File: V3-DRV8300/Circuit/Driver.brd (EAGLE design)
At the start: 63.5 x 55.5 mm, 37 parts, among them IC1 DRV8303DCA

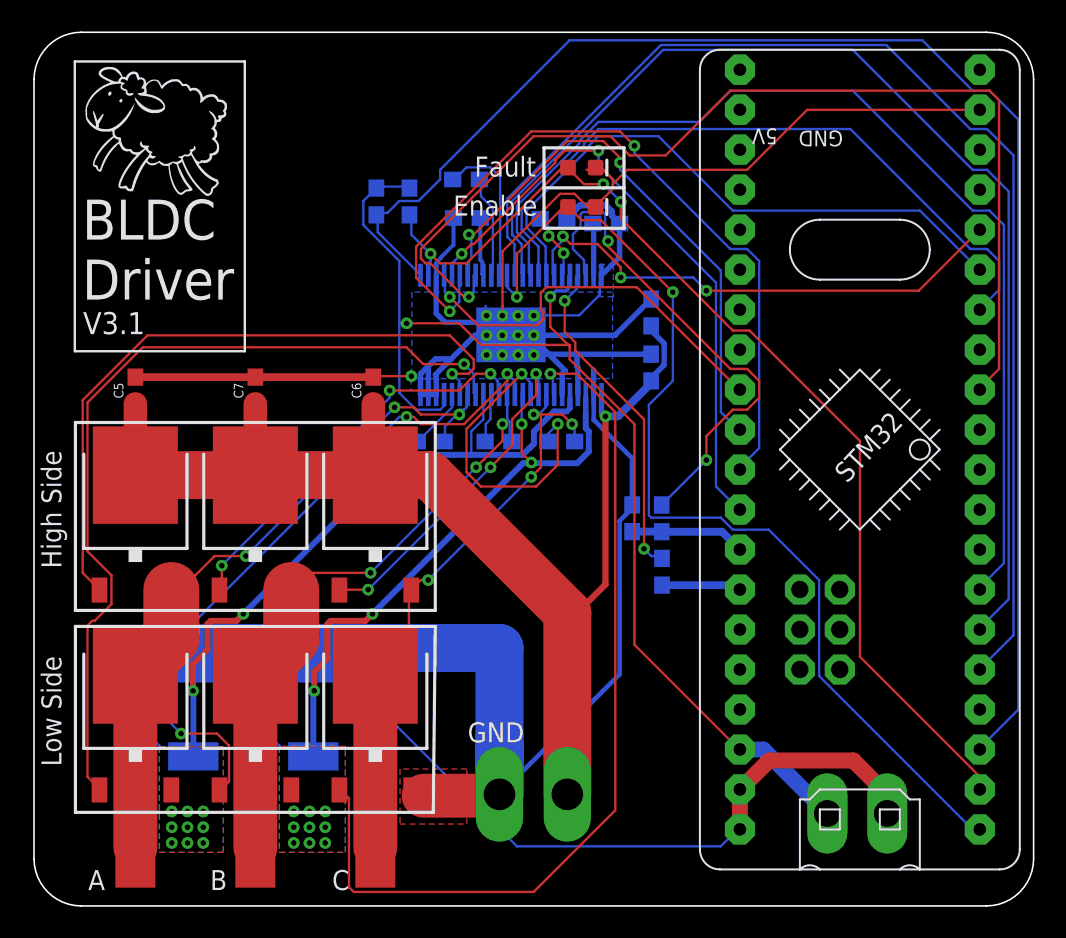
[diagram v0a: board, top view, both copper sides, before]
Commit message: Changed all the PWM output pin to the same timer, Added 2 selector for C.S.A.
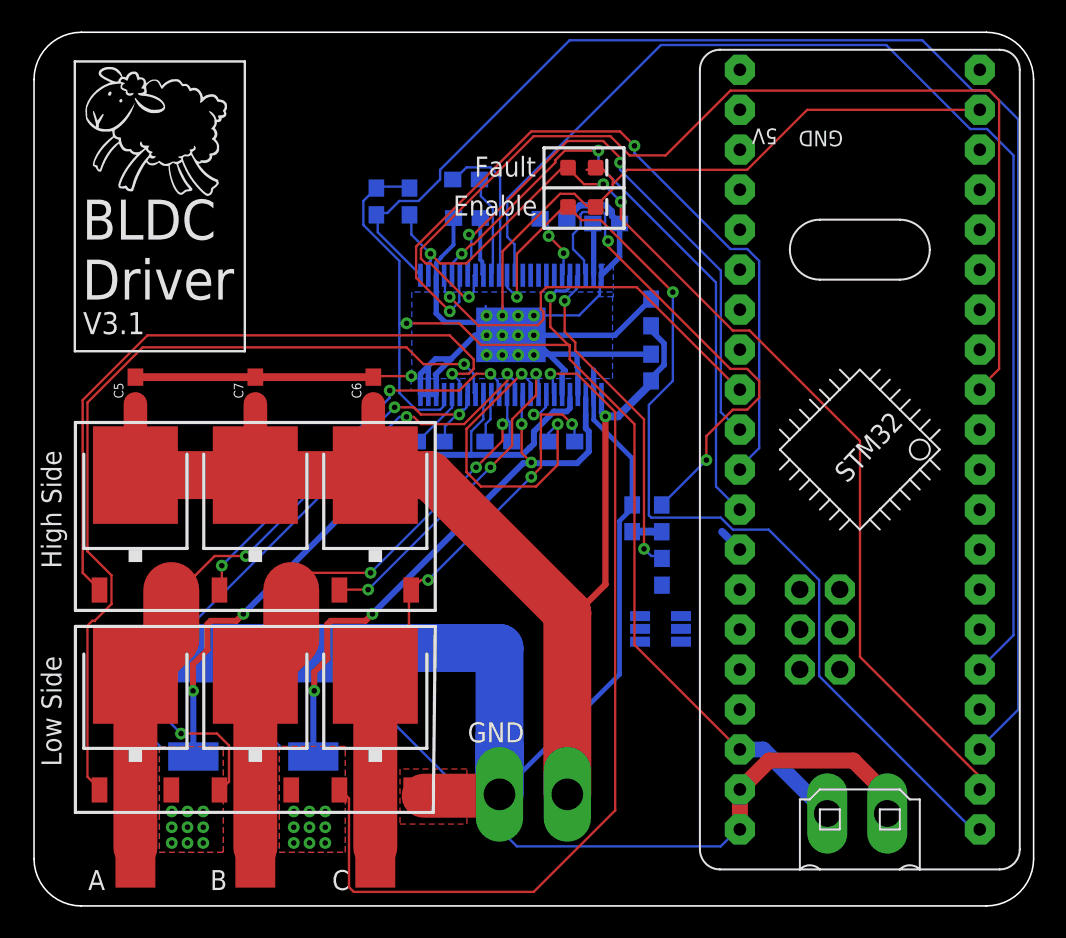
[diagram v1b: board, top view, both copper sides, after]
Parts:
- added SO1_SELECTOR, SO2_SELECTOR: JUMPER-SMT_3_2-NC_PASTE_SILK, SparkFun-Jumpers:SMT-JUMPER_3_2-NC_PASTE_SILK
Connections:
- new net SO1: R5.1, SO1_SELECTOR.2
- new net SO2: C16.1, R7.1, SO2_SELECTOR.2
- net PA1: now also SO1_SELECTOR.1
- net PA10: now also IC1.17; no longer IC1.15
- net PA11: now also SO1_SELECTOR.3
- net PA12: now also SO2_SELECTOR.3
- net PA2: now also SO2_SELECTOR.1
- net PA9: now also IC1.15; no longer IC1.14
- net PB0: no longer C16.1, R7.1
- net PB1: no longer R5.1
- net PB6: now also IC1.14; no longer IC1.16
- net PB7: now also IC1.16; no longer IC1.17
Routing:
- net PA9: track 72.8 -> 0.00 mm
- net PA10: track 66.1 -> 0.00 mm
- net PB6: track 44.3 -> 0.00 mm
- net PB7: track 39.0 -> 0.00 mm
- net PB8: track 32.7 -> 0.00 mm, vias 3 -> 0
- net PB0: track 7.31 -> 1.60 mm
- net PB1: track 5.15 -> 0.39 mm
- net SO2: track 0.00 -> 1.88 mm
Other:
- board text added: "|PA1| |SO1| |PA11|"
- board text added: "|PA2| |SO2| |PA12|"

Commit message: Ready for auto routering 2
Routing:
- net PA9: track 0.00 -> 63.0 mm, vias 0 -> 1
- net PA12: track 0.00 -> 54.3 mm
- net PB8: track 0.00 -> 51.0 mm
- net PA11: track 0.00 -> 47.1 mm
- net PB6: track 0.00 -> 46.9 mm
- net PB7: track 0.00 -> 46.4 mm
- net PA1: track 0.00 -> 25.7 mm, vias 0 -> 3
- net PA2: track 0.00 -> 25.2 mm, vias 0 -> 3
- net SO2: track 1.88 -> 10.7 mm
- net PA10: track 0.00 -> 7.32 mm, vias 0 -> 1
- net SO1: track 0.09 -> 3.63 mm

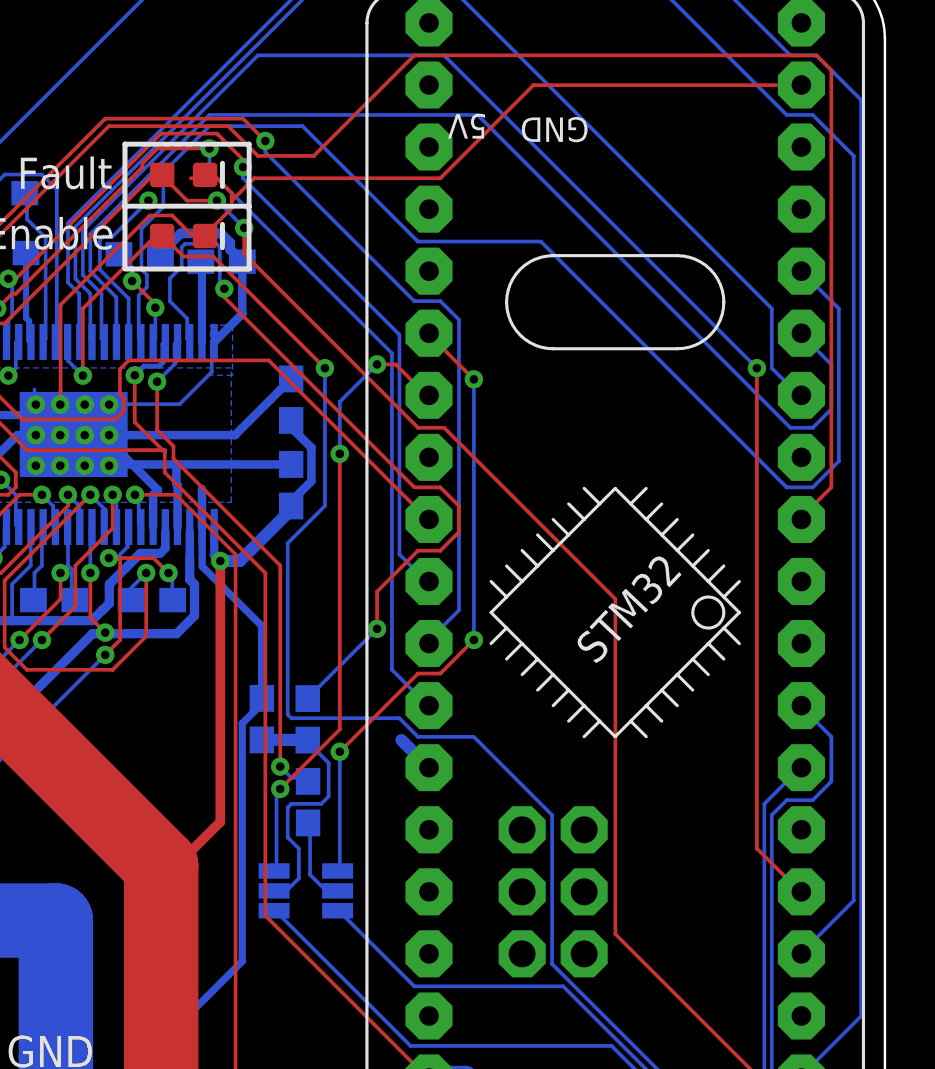
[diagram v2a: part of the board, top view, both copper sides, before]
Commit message: Routed all signal, ready for gerber gen
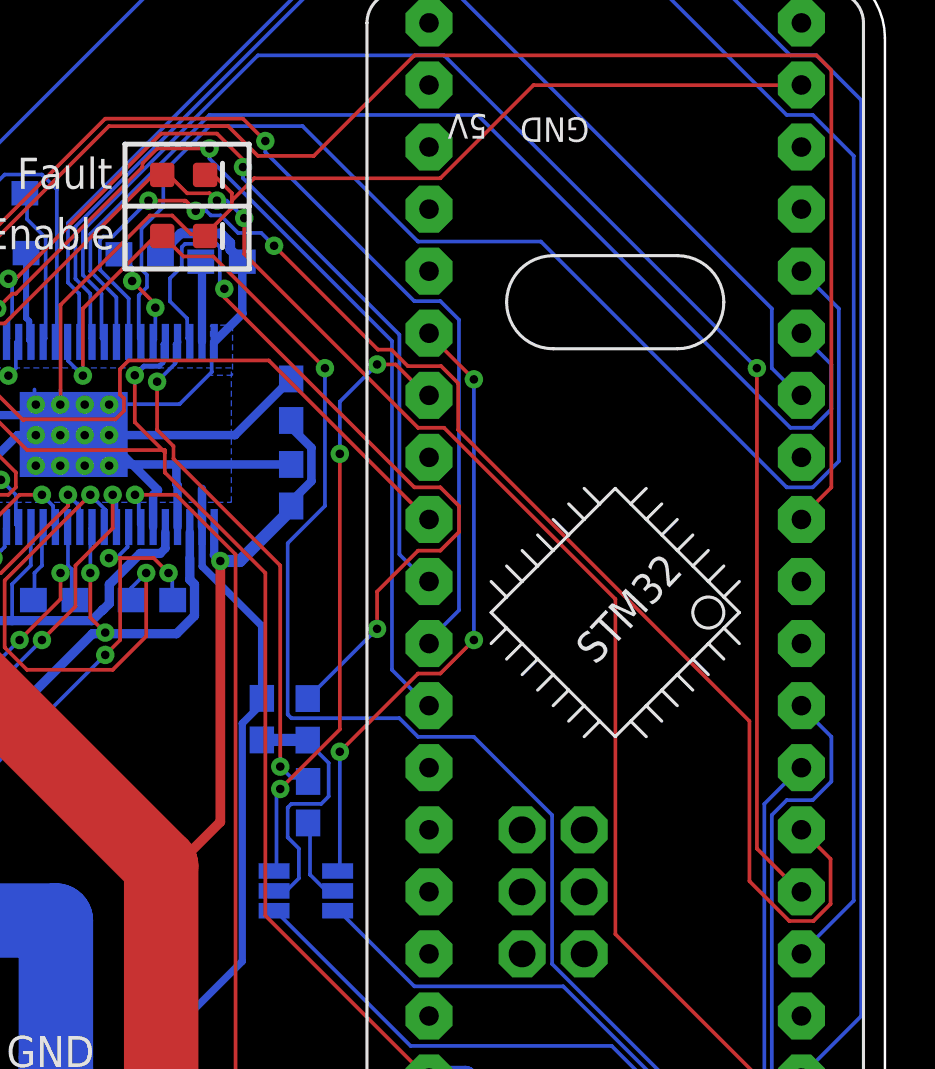
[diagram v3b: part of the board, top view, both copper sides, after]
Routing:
- net PA10: track 7.32 -> 56.2 mm, vias 1 -> 3
- net PB0: track 1.60 -> 0.00 mm
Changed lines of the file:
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@@
 <wire x1="13.4112" y1="32.1564" x2="13.543" y2="32.09935625" width="0.1524" layer="1"/>
 <wire x1="13.543" y1="32.09935625" x2="13.56" y2="32.092" width="0.1524" layer="1"/>
-<wire x1="34.5948" y1="45.2628" x2="35.052" y2="45.2628" width="0.1524" layer="1"/>
 <wire x1="35.052" y1="45.2628" x2="35.177" y2="45.4" width="0.1524" layer="1"/>
 <wire x1="21.1836" y1="32.1564" x2="21.174975" y2="32.152146875" width="0.1524" layer="1"/>
@@
 <signal name="PB1">
 <contactref element="U$1" pad="P$27"/>
-<wire x1="44.063" y1="18.878" x2="44.341" y2="18.6" width="0.5" layer="16"/>
 </signal>
 <signal name="PB0">
 <contactref element="U$1" pad="P$28"/>
-<wire x1="43.212" y1="22.269" x2="44.341" y2="21.14" width="0.5" layer="16"/>
 </signal>
 <signal name="PA7">
@@
 <wire x1="33.2232" y1="46.482" x2="32.6136" y2="45.8724" width="0.1524" layer="1"/>
 <wire x1="35.3568" y1="46.482" x2="33.2232" y2="46.482" width="0.1524" layer="1"/>
-<wire x1="35.3568" y1="45.5676" x2="35.3568" y2="46.482" width="0.1524" layer="16"/>
-<wire x1="42.8244" y1="38.1" x2="35.3568" y2="45.5676" width="0.1524" layer="16"/>
-<wire x1="42.8244" y1="25.146" x2="42.8244" y2="38.1" width="0.1524" layer="16"/>
+<wire x1="35.3568" y1="46.0676" x2="35.3568" y2="46.482" width="0.1524" layer="16"/>
+<wire x1="42.8244" y1="38.6" x2="35.3568" y2="46.0676" width="0.1524" layer="16"/>
+<wire x1="42.8244" y1="25.146" x2="42.8244" y2="38.6" width="0.1524" layer="16"/>
 <wire x1="44.196" y1="23.7744" x2="42.8244" y2="25.146" width="0.1524" layer="16"/>
 <wire x1="26.0604" y1="38.7096" x2="26.05" y2="38.565" width="0.1524" layer="16"/>
@@
 <wire x1="43.8912" y1="35.052" x2="44.958" y2="35.052" width="0.1524" layer="1"/>
 <wire x1="36.7784" y1="42.1648" x2="43.8912" y2="35.052" width="0.1524" layer="1"/>
-<wire x1="36.7784" y1="43.2316" x2="36.7784" y2="42.1648" width="0.1524" layer="1"/>
-<wire x1="35.6616" y1="44.3484" x2="36.7784" y2="43.2316" width="0.1524" layer="16"/>
-<wire x1="34.4424" y1="44.3484" x2="35.6616" y2="44.3484" width="0.1524" layer="1"/>
-<wire x1="33.528" y1="45.2628" x2="34.4424" y2="44.3484" width="0.1524" layer="1"/>
+<wire x1="36.7784" y1="43.6316" x2="36.7784" y2="42.1648" width="0.1524" layer="1"/>
+<wire x1="36.7784" y1="43.6316" x2="36.0616" y2="44.3484" width="0.1524" layer="16"/>
+<wire x1="35.6616" y1="44.3484" x2="36.0616" y2="44.3484" width="0.1524" layer="16"/>
+<wire x1="35.3616" y1="44.6484" x2="34.4424" y2="44.6484" width="0.1524" layer="1"/>
+<wire x1="35.3616" y1="44.6484" x2="35.6616" y2="44.3484" width="0.1524" layer="1"/>
+<wire x1="33.423" y1="45.4" x2="33.6908" y2="45.4" width="0.1524" layer="1"/>
+<wire x1="34.4424" y1="44.6484" x2="33.6908" y2="45.4" width="0.1524" layer="1"/>
 <wire x1="59.436" y1="5.9436" x2="59.581" y2="5.9" width="0.1524" layer="1"/>
-<wire x1="33.528" y1="45.2628" x2="33.423" y2="45.4" width="0.1524" layer="1"/>
 <via x="24.6888" y="39.9288" extent="1-16" drill="0.35"/>
-<via x="36.7784" y="43.2316" extent="1-16" drill="0.35"/>
+<via x="36.7784" y="43.6316" extent="1-16" drill="0.35"/>
 <via x="35.6616" y="44.3484" extent="1-16" drill="0.35"/>
 </signal>
@@
 <wire x1="32.05" y1="40.34" x2="30.8714" y2="41.5186" width="0.1524" layer="16"/>
 <wire x1="30.8714" y1="41.5186" x2="30.8714" y2="42.7446875" width="0.1524" layer="16"/>
-<wire x1="32.05" y1="38.565" x2="59.581" y2="18.6" width="0" layer="19" extent="16-16"/>
+<via x="34.7941625" y="43.9306" extent="1-16" drill="0.35"/>
+<wire x1="32.85935" y1="44.3456" x2="34.31414375" y2="44.3456" width="0.1524" layer="1"/>
+<wire x1="34.31414375" y1="44.3456" x2="34.31614375" y2="44.3436" width="0.1524" layer="1"/>
+<wire x1="34.31614375" y1="44.3436" x2="34.3811625" y2="44.3436" width="0.1524" layer="1"/>
+<wire x1="34.3811625" y1="44.3436" x2="34.7941625" y2="43.9306" width="0.1524" layer="1"/>
+<via x="38" y="42.5" extent="1-16" drill="0.35"/>
+<wire x1="34.7941625" y1="43.9306" x2="35.22125" y2="43.9306" width="0.1524" layer="16"/>
+<wire x1="35.22125" y1="43.9306" x2="35.41025" y2="43.7416" width="0.1524" layer="16"/>
+<wire x1="37.4752" y1="43.0248" x2="38" y2="42.5" width="0.1524" layer="16"/>
+<wire x1="36.52705" y1="43.0248" x2="37.4752" y2="43.0248" width="0.1524" layer="16"/>
+<wire x1="35.41025" y1="43.7416" x2="35.81025" y2="43.7416" width="0.1524" layer="16"/>
+<wire x1="35.81025" y1="43.7416" x2="36.52705" y2="43.0248" width="0.1524" layer="16"/>
+<wire x1="38" y1="42.5" x2="42.2504" y2="38.2496" width="0.1524" layer="1"/>
+<wire x1="44.83549375" y1="37.5738" x2="45.5348" y2="36.87449375" width="0.1524" layer="1"/>
+<wire x1="59.08650625" y1="14.8662" x2="60.07549375" y2="14.8662" width="0.1524" layer="1"/>
+<wire x1="60.07549375" y1="14.8662" x2="60.7748" y2="15.56550625" width="0.1524" layer="1"/>
+<wire x1="45.5348" y1="34.9652" x2="57.4548" y2="23.0452" width="0.1524" layer="1"/>
+<wire x1="43.47685625" y1="37.5738" x2="44.83549375" y2="37.5738" width="0.1524" layer="1"/>
+<wire x1="45.5348" y1="36.87449375" x2="45.5348" y2="34.9652" width="0.1524" layer="1"/>
+<wire x1="42.2504" y1="38.2496" x2="42.80105625" y2="38.2496" width="0.1524" layer="1"/>
+<wire x1="42.80105625" y1="38.2496" x2="43.47685625" y2="37.5738" width="0.1524" layer="1"/>
+<wire x1="57.4548" y1="23.0452" x2="57.4548" y2="16.49790625" width="0.1524" layer="1"/>
+<wire x1="57.4548" y1="16.49790625" x2="59.08650625" y2="14.8662" width="0.1524" layer="1"/>
+<wire x1="60.7748" y1="17.4062" x2="59.581" y2="18.6" width="0.1524" layer="1"/>
+<wire x1="60.7748" y1="15.56550625" x2="60.7748" y2="17.4062" width="0.1524" layer="1"/>
 </signal>
 <signal name="PA11">

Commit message: Fixed a little mistake/bug (PA2 -> PA0)
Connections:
- net PA0: now also SO2_SELECTOR.1
- net PA2: no longer SO2_SELECTOR.1
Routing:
- net PA0: track 0.00 -> 29.9 mm, vias 0 -> 2
- net PA2: track 25.2 -> 0.00 mm, vias 3 -> 0
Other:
- board text added: "|PA0| |SO2| |PA12|"
- board text removed: "|PA2| |SO2| |PA12|"
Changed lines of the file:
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@@
 <wire x1="-0.5" y1="51" x2="2.5" y2="54" width="0.1" layer="20" curve="-90"/>
 <wire x1="37" y1="41.55" x2="31.9" y2="41.55" width="0.2032" layer="21"/>
-<text x="38.9" y="12" size="0.5" layer="26" font="vector" rot="MR0">|PA2|
+<text x="38.9" y="12" size="0.5" layer="26" font="vector" rot="MR0">|PA0|
 |SO2|
 |PA12|</text>
@@
 <signal name="PA2">
 <contactref element="U$1" pad="P$34"/>
-<contactref element="SO2_SELECTOR" pad="1"/>
-<wire x1="38.1" y1="20.1168" x2="38.1" y2="16.9164" width="0.1524" layer="16"/>
-<wire x1="38.2524" y1="20.2692" x2="38.1" y2="20.1168" width="0.1524" layer="16"/>
-<wire x1="40.6908" y1="22.7076" x2="38.2524" y2="20.2692" width="0.1524" layer="1"/>
-<wire x1="40.6908" y1="33.9852" x2="40.6908" y2="22.7076" width="0.1524" layer="1"/>
-<wire x1="40.6908" y1="36.1188" x2="40.6908" y2="33.9852" width="0.1524" layer="16"/>
-<wire x1="42.2148" y1="37.6428" x2="40.6908" y2="36.1188" width="0.1524" layer="16"/>
-<wire x1="42.9768" y1="37.6428" x2="42.2148" y2="37.6428" width="0.1524" layer="1"/>
-<wire x1="44.196" y1="36.4236" x2="42.9768" y2="37.6428" width="0.1524" layer="1"/>
-<wire x1="38.1" y1="16.9164" x2="38" y2="16.9128" width="0.1524" layer="16"/>
-<wire x1="44.196" y1="36.4236" x2="44.341" y2="36.38" width="0.1524" layer="1"/>
-<via x="38.2524" y="20.2692" extent="1-16" drill="0.35"/>
-<via x="40.6908" y="33.9852" extent="1-16" drill="0.35"/>
-<via x="42.2148" y="37.6428" extent="1-16" drill="0.35"/>
 </signal>
 <signal name="PA1">
@@
 <signal name="PA0">
 <contactref element="U$1" pad="P$36"/>
+<contactref element="SO2_SELECTOR" pad="1"/>
+<wire x1="38.1" y1="20.1168" x2="38.1" y2="16.9164" width="0.1524" layer="16"/>
+<wire x1="38.2524" y1="20.2692" x2="38.1" y2="20.1168" width="0.1524" layer="16"/>
+<wire x1="43.1292" y1="25.146" x2="38.2524" y2="20.2692" width="0.1524" layer="1"/>
+<wire x1="43.1292" y1="26.8224" x2="43.1292" y2="25.146" width="0.1524" layer="1"/>
+<wire x1="43.7388" y1="27.432" x2="43.1292" y2="26.8224" width="0.1524" layer="1"/>
+<wire x1="44.8056" y1="27.432" x2="43.7388" y2="27.432" width="0.1524" layer="1"/>
+<wire x1="46.7868" y1="29.4132" x2="44.8056" y2="27.432" width="0.1524" layer="1"/>
+<wire x1="46.7868" y1="39.0144" x2="46.7868" y2="29.4132" width="0.1524" layer="16"/>
+<wire x1="44.3484" y1="41.4528" x2="46.7868" y2="39.0144" width="0.1524" layer="16"/>
+<wire x1="38.1" y1="16.9164" x2="38" y2="16.9128" width="0.1524" layer="16"/>
+<wire x1="44.3484" y1="41.4528" x2="44.341" y2="41.46" width="0.1524" layer="16"/>
+<via x="38.2524" y="20.2692" extent="1-16" drill="0.35"/>
+<via x="46.7868" y="29.4132" extent="1-16" drill="0.35"/>
 </signal>
 <signal name="PC15">
@@
 <wire x1="24.0792" y1="40.2336" x2="24.0792" y2="39.624" width="0.1524" layer="1"/>
 <wire x1="31.242" y1="47.3964" x2="24.0792" y2="40.2336" width="0.1524" layer="1"/>
-<wire x1="36.1188" y1="47.3964" x2="35.3" y2="47.3964" width="0.1524" layer="1"/>
-<wire x1="35.3" y1="47.3964" x2="31.242" y2="47.3964" width="0.1524" layer="1"/>
+<wire x1="36.1188" y1="47.3964" x2="31.242" y2="47.3964" width="0.1524" layer="1"/>
 <wire x1="37.338" y1="46.1772" x2="36.1188" y2="47.3964" width="0.1524" layer="1"/>
 <wire x1="39.624" y1="46.1772" x2="37.338" y2="46.1772" width="0.1524" layer="1"/>
